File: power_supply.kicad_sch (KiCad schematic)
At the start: 16 parts, among them U401 TPS62170DSG, U402 MIC5365-3.3YD5

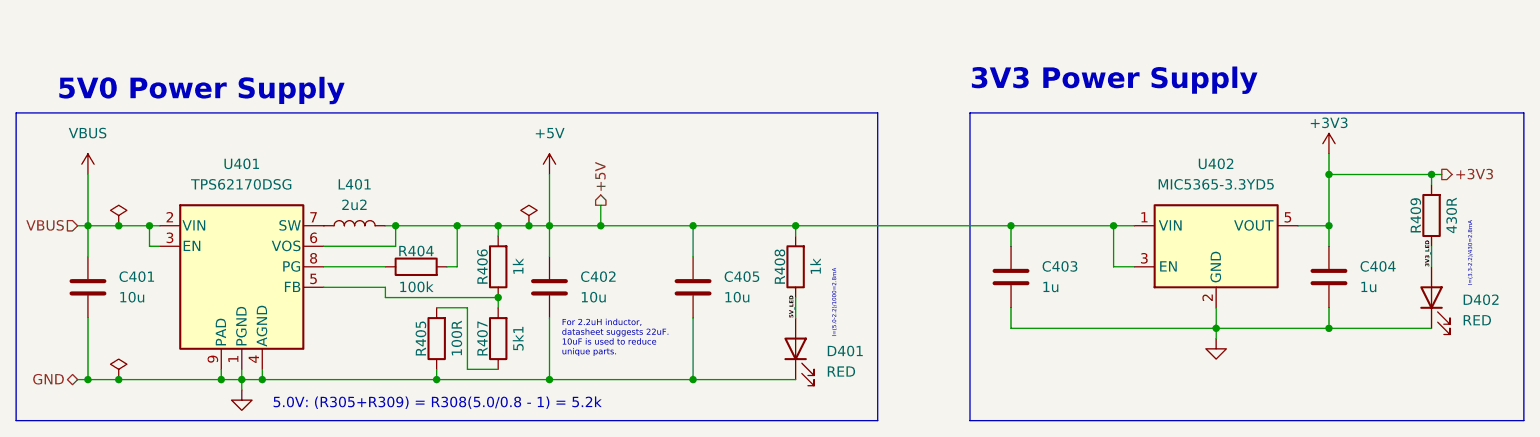
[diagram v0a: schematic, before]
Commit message: Changed motor power supply
Removed 5V power rail. Migrated 3.3V rail to TPS62160
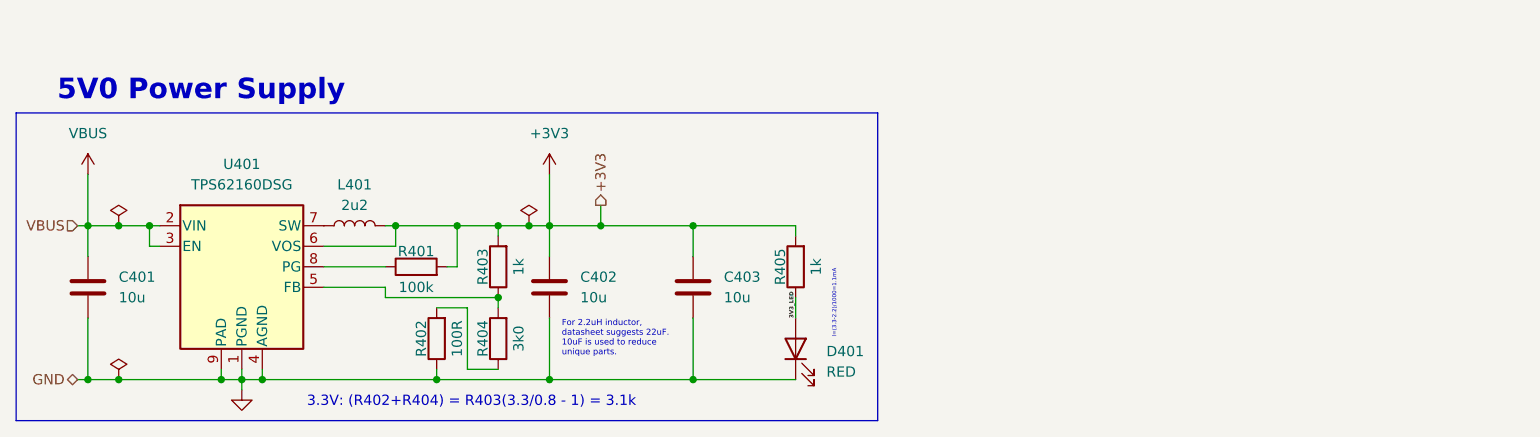
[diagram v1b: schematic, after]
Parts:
- removed C403, C404: 1u, Capacitor_SMD:C_0603_1608Metric, symbol Device:C
- removed D402: RED, LED_SMD:LED_0603_1608Metric, symbol Device:LED
- removed R409: 430R, Resistor_SMD:R_0603_1608Metric, symbol Device:R
- removed U402: MIC5365-3.3YD5, Package_TO_SOT_SMD:SOT-23-5, symbol Regulator_Linear:MIC5365-3.3YD5
- R404: renamed from R407; value 5k1 -> 3k0
- U401: value TPS62170DSG -> TPS62160DSG
- renumbered C405 to C403, R404 to R401, R405 to R402, R406 to R403, R408 to R405
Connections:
- net +5V is gone; now on net +3V3: C402.1, C403.1, L401.2, R401.2, R403.2, R405.2, U401.6 (VOS)
- net 5V_LED is gone; now on net 3V3_LED: D401.2 (A), R405.1
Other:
- note added: "3.3V: (R402+R404) = R403(3.3/0.8 - 1) = 3.1k"
- note added: "I=(3.3-2.2)/1000=1.1mA"
- note removed: "3V3 Power Supply"
- note removed: "5.0V: (R305+R309) = R308(5.0/0.8 - 1) = 5.2k"
- note removed: "I=(3.3-2.2)/430=2.8mA"
- note removed: "I=(5.0-2.2)/1000=2.8mA"

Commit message: Finished Rev A1 PCB
Added all components and routed parts for Rev A1 PCB
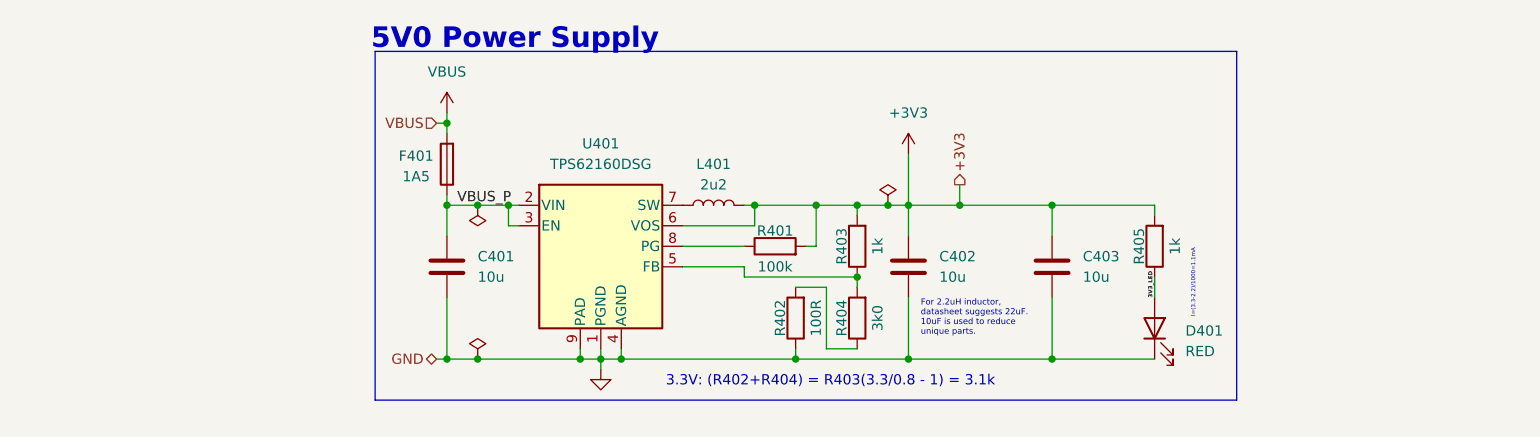
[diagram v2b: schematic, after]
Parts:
- added F401: 1A5, Fuse:Fuseholder_Littelfuse_Nano2_154x, symbol Device:Fuse
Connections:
- net VBUS: now also F401.2; no longer C401.1, U401.2 (VIN), U401.3 (EN)
- new net VBUS_P: C401.1, F401.1, U401.2 (VIN), U401.3 (EN)
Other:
- moved on the sheet: C401, C402, C403, D401, L401, R401, R402, R403, R404, R405, U401
